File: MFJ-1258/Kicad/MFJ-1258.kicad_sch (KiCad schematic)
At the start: 19 parts, among them J1 C64-UserPort, J2 Screw_Terminal_01x01, J3 Screw_Terminal_01x01, Q1 2N3906, Q2 2N3906, Q3 2N3906, U1 NE555P

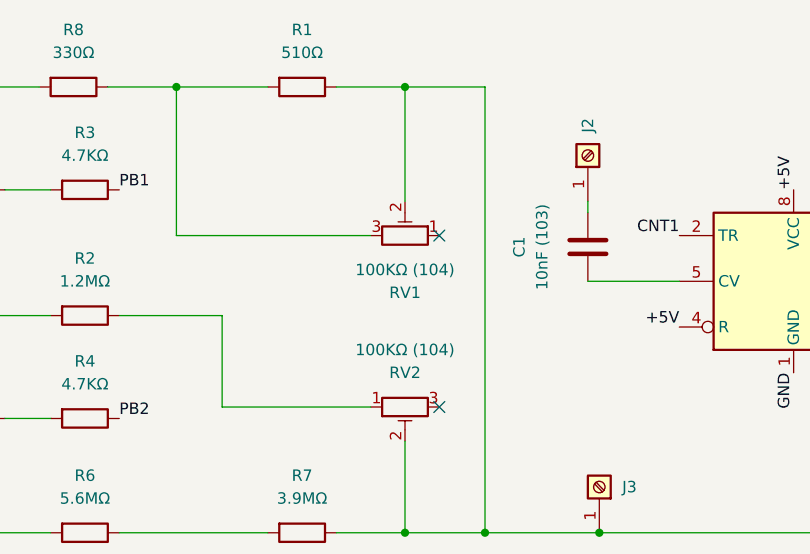
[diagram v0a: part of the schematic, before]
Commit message: Corrected RV1 value
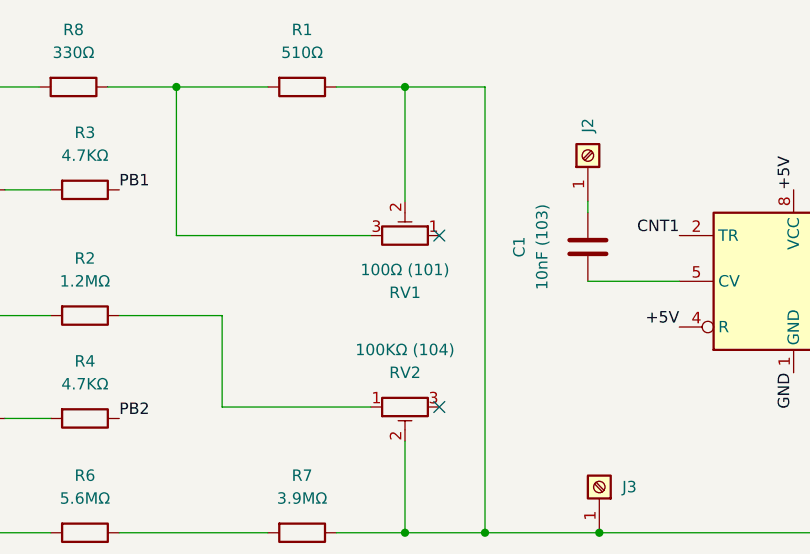
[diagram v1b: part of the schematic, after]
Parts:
- RV1: value 100KΩ (104) -> 100Ω (101)
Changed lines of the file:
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@@
       (effects (font (size 1.27 1.27)))
     )
-    (property "Value" "100KΩ (104)" (at 162.56 91.44 90)
+    (property "Value" "100Ω (101)" (at 162.56 91.44 90)
       (effects (font (size 1.27 1.27)))
     )

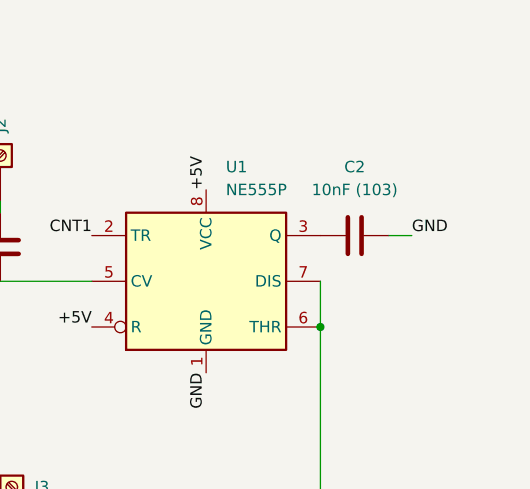
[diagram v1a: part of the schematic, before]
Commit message: Forgot to connect PB7 pin
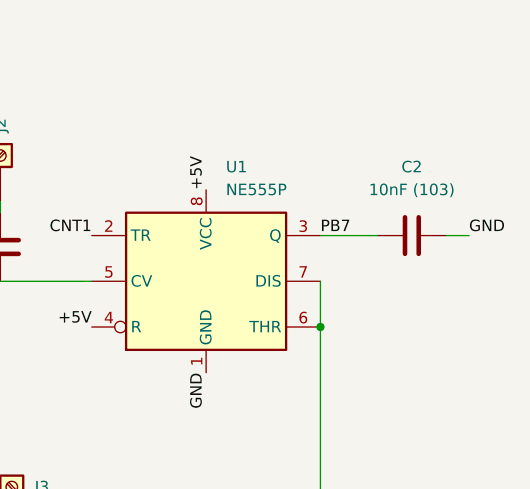
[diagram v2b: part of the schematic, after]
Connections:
- net PB7: now also C2.2, U1.3 (Q)
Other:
- moved on the sheet: C2
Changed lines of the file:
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@@
+    (stroke (width 0) (type default))
+  )
+  (wire (pts (xy 224.79 87.63) (xy 218.44 87.63))
     (stroke (width 0) (type default))
   )
@@
     (stroke (width 0) (type default))
   )
-  (wire (pts (xy 226.06 87.63) (xy 228.6 87.63))
+  (wire (pts (xy 232.41 87.63) (xy 234.95 87.63))
     (stroke (width 0) (type default))
   )
@@
     (effects (font (size 1.27 1.27)) (justify left bottom))
   )
+  (label "PB7" (at 218.44 87.63 0) (fields_autoplaced)
+    (effects (font (size 1.27 1.27)) (justify left bottom))
+  )
   (label "GND" (at 205.74 102.87 270) (fields_autoplaced)
     (effects (font (size 1.27 1.27)) (justify right bottom))
@@
     (effects (font (size 1.27 1.27)) (justify right bottom))
   )
-  (label "GND" (at 228.6 87.63 0) (fields_autoplaced)
+  (label "GND" (at 234.95 87.63 0) (fields_autoplaced)
     (effects (font (size 1.27 1.27)) (justify left bottom))
   )
@@
     )
   )
-  (symbol (lib_id "Device:C") (at 222.25 87.63 270) (unit 1)
-    (in_bom yes) (on_board yes) (dnp no) (fields_autoplaced)
-    (property "Reference" "C2" (at 222.25 80.01 90)
-      (effects (font (size 1.27 1.27)))
-    )
-    (property "Value" "10nF (103)" (at 222.25 82.55 90)
-      (effects (font (size 1.27 1.27)))
-    )
-    (property "Footprint" "Capacitor_THT:C_Disc_D5.0mm_W2.5mm_P2.50mm" (at 218.44 88.5952 0)
-      (effects (font (size 1.27 1.27)) hide)
-    )
-    (property "Datasheet" "~" (at 222.25 87.63 0)
-      (effects (font (size 1.27 1.27)) hide)
-    )
+  (symbol (lib_id "Device:C") (at 228.6 87.63 270) (unit 1)
+    (in_bom yes) (on_board yes) (dnp no) (fields_autoplaced)
+    (property "Reference" "C2" (at 228.6 80.01 90)
+      (effects (font (size 1.27 1.27)))
+    )
+    (property "Value" "10nF (103)" (at 228.6 82.55 90)
+      (effects (font (size 1.27 1.27)))
+    )
+    (property "Footprint" "Capacitor_THT:C_Disc_D5.0mm_W2.5mm_P2.50mm" (at 224.79 88.5952 0)
+      (effects (font (size 1.27 1.27)) hide)
+    )
+    (property "Datasheet" "~" (at 228.6 87.63 0)
+      (effects (font (size 1.27 1.27)) hide)
+    )
